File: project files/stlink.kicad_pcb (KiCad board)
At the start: 2 copper layers, 38.1 x 17.8 mm, 55 parts, among them J1 USB_C_Receptacle_USB2.0, J2 Sides, J3 SWD, Q1 MMBT9013, U1 STM32F103CBTx, U2 AMS1117-3.3, Y1 8MHz

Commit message: updates
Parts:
- removed C3: 20pF, Capacitor_SMD:C_0603_1608Metric
- removed R3: 100R, Resistor_SMD:R_0603_1608Metric_Pad1.05x0.95mm_HandSolder
- added C11: 22uF, Capacitor_Tantalum_SMD:CP_EIA-7343-30_AVX-N, B.Cu at (99.8, 166.4)
- added C7: 22uF, Capacitor_Tantalum_SMD:CP_EIA-7343-30_AVX-N, B.Cu at (99.8, 153.7)
- added F1: 1A, Fuse:Fuse_1210_3225Metric, B.Cu at (100.3, 118.0)
- added J4: TARGET, Connector_PinHeader_2.54mm:PinHeader_1x12_P2.54mm_Vertical, B.Cu at (105.4, 110.5)
- D1, D4, U2: moved to B.Cu
- J2: value Sides -> SELF; footprint Package_DIP:DIP-24_W15.24mm_Socket -> Connector_PinHeader_2.54mm:PinHeader_1x12_P2.54mm_Vertical; moved to B.Cu
- moved D1 60.6 mm to (101.6, 125.7), turned to 180 degrees
- moved U2 19.4 mm to (99.7, 160.0), turned to 180 degrees
- turned J2 to 270 degrees
- turned U1 to 180 degrees
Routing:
- net /D-: track 0.00 -> 2.72 mm
- net /D+: track 0.00 -> 2.71 mm

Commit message: ajfdlsa;jd;sakd
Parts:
- F1: footprint Fuse:Fuse_1210_3225Metric -> Fuse:Fuse_1206_3216Metric
- moved D3 56.5 mm to (100.3, 124.5)
- moved R12 56.3 mm to (100.3, 125.7)
- moved C13 28.1 mm to (121.0, 142.2)
- moved R6 23.2 mm to (133.7, 144.8)
- moved R5 13.7 mm to (133.7, 149.9)
- moved D1 5.02 mm to (100.3, 120.9), turned to 90 degrees
- moved F1 1.14 mm to (100.3, 116.8)
- turned R8 to 180 degrees
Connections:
- J2 pad 3: Self_SWDIOh -> Self_SWDCLKh
- J2 pad 5: Self_SWDCLKh -> Self_SWDIOh
- J4 pad 10: T_SWDCLKh -> T_SWDIOh
- J4 pad 11: T_SWOh -> T_NRST_SWDh
- J4 pad 12: T_NRST_SWDh -> T_SWOh
- J4 pad 8: T_SWDIOh -> T_SWDCLKh

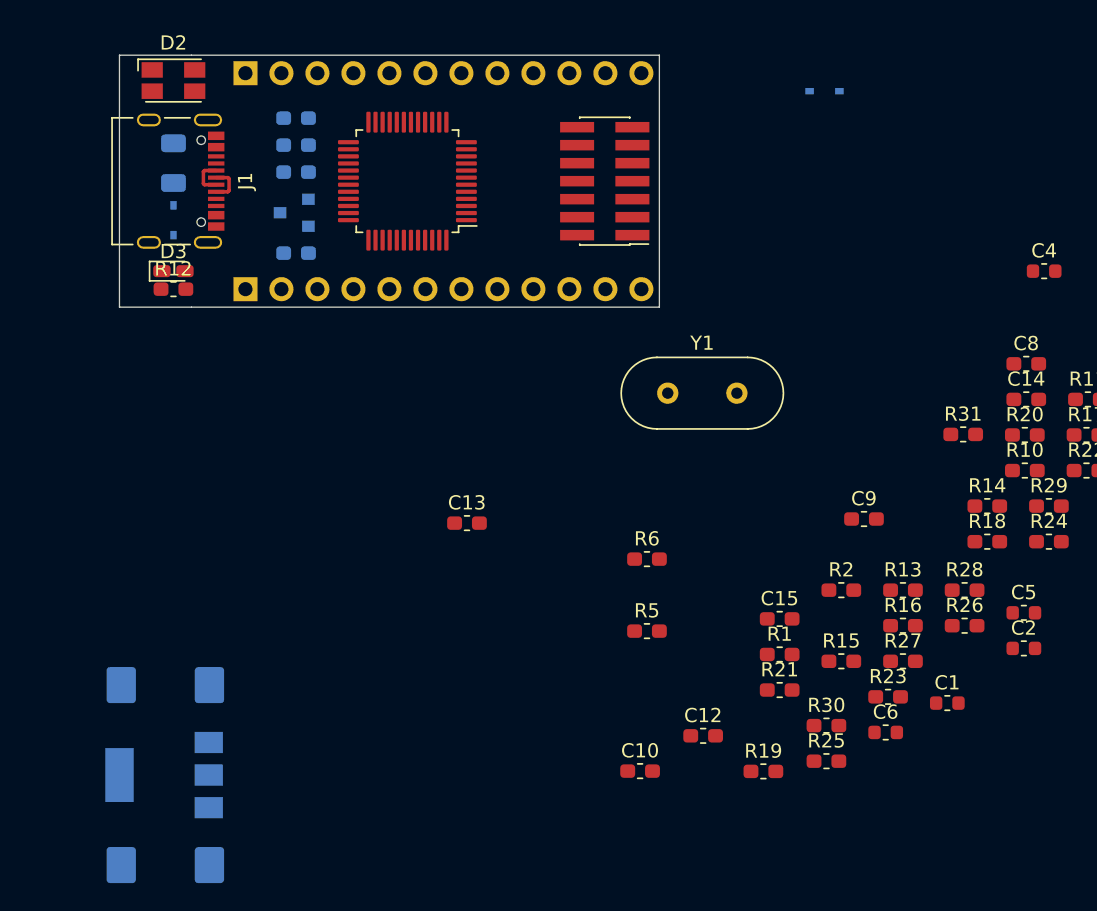
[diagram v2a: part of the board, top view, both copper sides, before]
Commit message: Added JTAG to STDC14
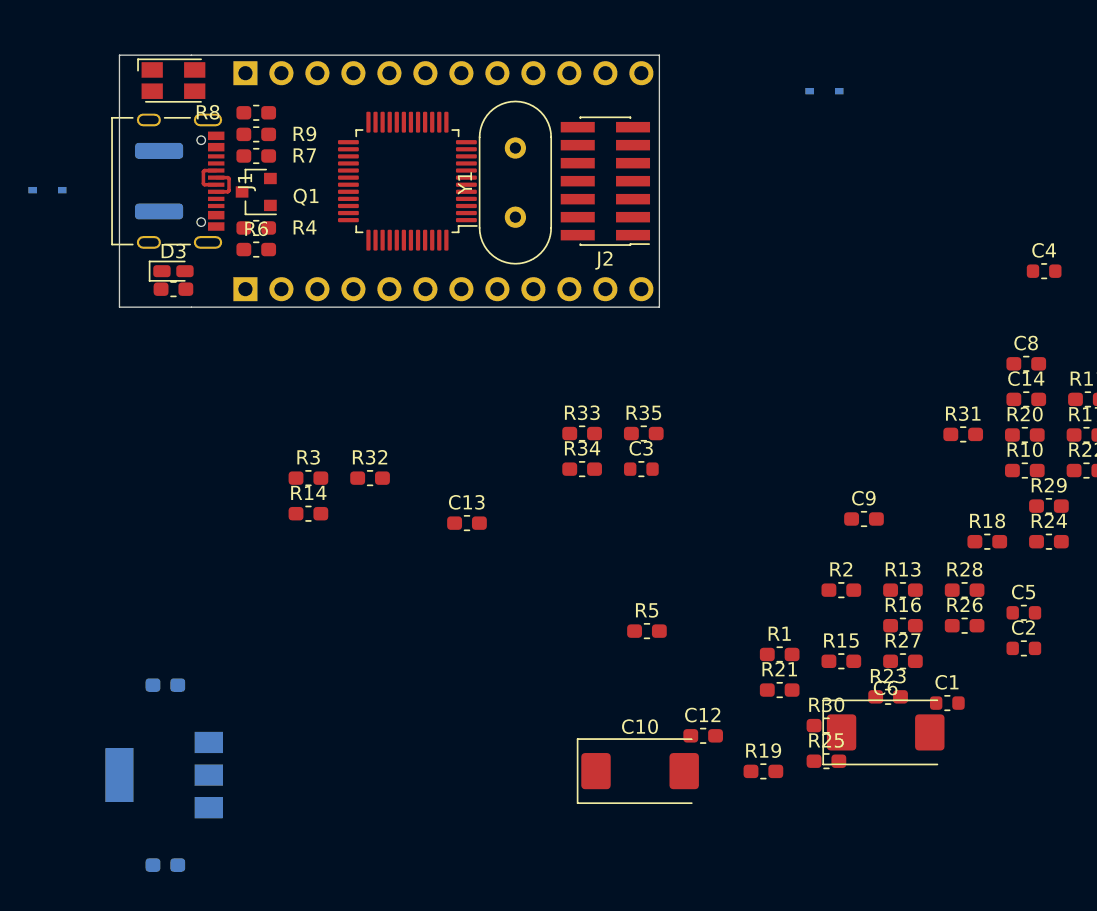
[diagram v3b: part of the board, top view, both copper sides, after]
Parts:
- removed C15: 100nF, Capacitor_SMD:C_0603_1608Metric_Pad1.05x0.95mm_HandSolder
- added C3: 100nF, Capacitor_SMD:C_0603_1608Metric, F.Cu at (133.3, 138.4)
- added R3: 10R, Resistor_SMD:R_0603_1608Metric_Pad1.05x0.95mm_HandSolder, F.Cu at (109.9, 139.1)
- added R32: 47R, Resistor_SMD:R_0603_1608Metric_Pad1.05x0.95mm_HandSolder, F.Cu at (114.2, 139.1)
- added R33: 47R, Resistor_SMD:R_0603_1608Metric_Pad1.05x0.95mm_HandSolder, F.Cu at (129.2, 135.9)
- added R34: 22R, Resistor_SMD:R_0603_1608Metric_Pad1.05x0.95mm_HandSolder, F.Cu at (129.2, 138.4)
- added R35: 22R, Resistor_SMD:R_0603_1608Metric_Pad1.05x0.95mm_HandSolder, F.Cu at (133.5, 135.9)
- C10: value 12pF -> 22uF; footprint Capacitor_SMD:C_0603_1608Metric_Pad1.05x0.95mm_HandSolder -> Capacitor_Tantalum_SMD:CP_EIA-7343-30_AVX-N
- C11: value 22uF -> 100nF; footprint Capacitor_Tantalum_SMD:CP_EIA-7343-30_AVX-N -> Capacitor_SMD:C_0603_1608Metric_Pad1.05x0.95mm_HandSolder
- C6: value 100nF -> 22uF; footprint Capacitor_SMD:C_0603_1608Metric -> Capacitor_Tantalum_SMD:CP_EIA-7343-30_AVX-N
- C7: value 22uF -> 12pF; footprint Capacitor_Tantalum_SMD:CP_EIA-7343-30_AVX-N -> Capacitor_SMD:C_0603_1608Metric_Pad1.05x0.95mm_HandSolder
- C8: value 12pF -> 100nF
- C9: value 100nF -> 12pF
- F1: footprint Fuse:Fuse_1206_3216Metric -> Fuse:Fuse_1812_4532Metric
- J2: value SELF -> SWD; footprint Connector_PinHeader_2.54mm:PinHeader_1x12_P2.54mm_Vertical -> Connector_PinHeader_1.27mm:PinHeader_2x07_P1.27mm_Vertical_SMD; moved to F.Cu
- J3: value SWD -> SELF; footprint Connector_PinHeader_1.27mm:PinHeader_2x07_P1.27mm_Vertical_SMD -> Connector_PinHeader_2.54mm:PinHeader_1x12_P2.54mm_Vertical; moved to B.Cu
- Q1, R4: moved to F.Cu
- R10: value 330R -> 36K
- R12: value 1K -> 330R
- R14: value 100K -> 1K
- R20, R21: value 220R -> 22R
- R22: value 100R -> 22R
- R23: value 10K -> 22R
- R24: value 10K -> 100R
- R25: value 680R -> 22R
- R26, R27: value 47R -> 220R
- R28: value 22R -> 680R
- R29, R30: value 22R -> 10K
- R7: value 10K -> 10R; moved to F.Cu
- R8: value 100R -> 10K; moved to F.Cu
- R9: value 36K -> 100R; moved to F.Cu
- moved R14 47.9 mm to (109.9, 141.6)
- moved R6 35.2 mm to (106.2, 122.9)
- moved J2 26.5 mm to (130.8, 118.1), turned to 180 degrees
- moved J3 26.5 mm to (105.4, 125.7), turned to 270 degrees
- moved Y1 16.4 mm to (124.5, 120.7), turned to 90 degrees
- moved D1 9.14 mm to (91.4, 118.7), turned to 180 degrees
- moved R4 3.32 mm to (106.2, 121.4)
- moved Q1 3.06 mm to (106.2, 118.9)
- moved R7 3.03 mm to (106.2, 116.3)
- moved R9 2.91 mm to (106.2, 114.8)
- moved R8 2.83 mm to (106.2, 113.3)
- moved F1 1.63 mm to (99.3, 118.1)
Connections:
- net Net-(U1-Pad19) renamed /T_JRST
- C10 pad 1: /STLINK_OST_OUT -> +3V3
- C12 pad 1: +3V3 -> BOOT_0h
- C13 pad 1: BOOT_0h -> Self_NRSTh
- C14 pad 1: Self_NRSTh -> /AIN
- C6 pad 1: +3V3 -> +5V
- C7 pad 1: +5V -> /STLINK_OSC_IN
- C8 pad 1: /STLINK_OSC_IN -> +5V
- C9 pad 1: +5V -> /STLINK_OST_OUT
- J2 pad 1: +5V -> Net-(J2-Pad1)
- J2 pad 10: Self_RXh -> T_JTDI(h)
- J2 pad 11: Self_TXh -> GND_detect(h)
- J2 pad 12: GNDREF -> T_NRST_SWDh
- J2 pad 2: +3V3 -> Net-(J2-Pad2)
- J2 pad 3: Self_SWDCLKh -> T_Vref
- J2 pad 4: GNDREF -> T_JTMS-T_SWDIO(h)
- J2 pad 5: Self_SWDIOh -> GNDREF
- J2 pad 6: Self_NRSTh -> T_JTLK(h)
- J2 pad 7: Self_SWOh -> GNDREF
- J2 pad 8: BOOT_0h -> T_JTDO-T_SWO(h)
- J2 pad 9: +3V3 -> T_JTLK(h)
- J3 pad 1: Net-(J3-Pad1) -> +5V
- J3 pad 10: Net-(J3-Pad10) -> Self_RXh
- J3 pad 11: GNDREF -> Self_TXh
- J3 pad 12: T_NRST_SWDh -> GNDREF
- J3 pad 2: Net-(J3-Pad2) -> +3V3
- J3 pad 3: T_Vref -> Self_SWDCLKh
- J3 pad 4: T_SWDIOh -> GNDREF
- J3 pad 5: GNDREF -> Self_SWDIOh
- J3 pad 6: T_SWDCLKh -> Self_NRSTh
- J3 pad 7: GNDREF -> Self_SWOh
- J3 pad 8: Net-(J3-Pad8) -> BOOT_0h
- J3 pad 9: Net-(J3-Pad9) -> +3V3
- R10 pad 1: Net-(D2-Pad3) -> GNDREF
- R10 pad 2: Self_TXh -> Net-(Q1-Pad1)
- R11 pad 1: Net-(D2-Pad1) -> Net-(D2-Pad3)
- R11 pad 2: Self_TXh -> /STLINK_LED
- R12 pad 1: Net-(D3-Pad2) -> Net-(D2-Pad1)
- R12 pad 2: +3V3 -> /STLINK_LED
- R13 pad 2: +3V3 -> GNDREF
- R14 pad 1: GNDREF -> Net-(D3-Pad2)
- R14 pad 2: /BOOT_1 -> +3V3
- R20 pad 1: /T_SWIM_IN -> T_NRST_SWDh
- R20 pad 2: /T_SWIM -> /T_NRST_SWD
- R21 pad 1: /T_NRST_SWIM_IN -> T_JTLK(h)
- R21 pad 2: /T_NRST_SWIM -> /T_JTCK
- R22 pad 1: /T_SWDIO_IN -> T_JTDO-T_SWO(h)
- R22 pad 2: /T_SWDIO -> /T_SWO
- R23 pad 1: /PC13 -> T_JTDO-T_SWO(h)
- R23 pad 2: GNDREF -> /T_JTDO
- R24 pad 1: /PC14 -> /T_SWDIO_IN
- R24 pad 2: GNDREF -> /T_JTMS
- R25 pad 1: /T_SWIM -> T_JTDI(h)
- R25 pad 2: +3V3 -> /T_JTDI
- R26 pad 1: /T_SWIM -> /T_SWIM_IN
- R26 pad 2: T_SWIMh -> /T_SWIM
- R27 pad 1: /T_NRST_SWIM -> /T_NRST_SWIM_IN
- R27 pad 2: T_NRST_SWIMh -> /T_NRST_SWIM
- R28 pad 1: T_NRST_SWDh -> /T_SWIM
- R28 pad 2: /T_NRST_SWD -> +3V3
- R29 pad 1: T_SWDCLKh -> /PC13
- R29 pad 2: /T_SWDCLK -> GNDREF
- R30 pad 1: T_SWDIOh -> /PC14
- R30 pad 2: /T_SWDIO -> GNDREF
- R31 pad 1: T_SWOh -> T_JTMS-T_SWDIO(h)
- R31 pad 2: Self_RXh -> /T_JTMS
- R7 pad 1: +5V -> /T_SWO
- R7 pad 2: Net-(Q1-Pad1) -> Self_RXh
- R8 pad 1: /USB_RENUMn -> +5V
- R9 pad 1: GNDREF -> /USB_RENUMn
- U1 pad 12: T_VCP_RXh -> /STLINK_TX
- U1 pad 13: T_VCP_TXh -> /STLINK_RX
- U1 pad 15: /T_SWDCLK -> /T_JTCK
- U1 pad 16: Net-(U1-Pad16) -> /T_JTDO
- U1 pad 17: Net-(U1-Pad17) -> /T_JTDI
- U1 pad 20: /BOOT_1 -> GNDREF
- U1 pad 26: /T_SWDCLK -> /T_JTCK
- U1 pad 27: /T_SWDIO -> /T_JTMS
- U1 pad 41: /T_SWIM_IN -> /T_NRST_SWIM_IN

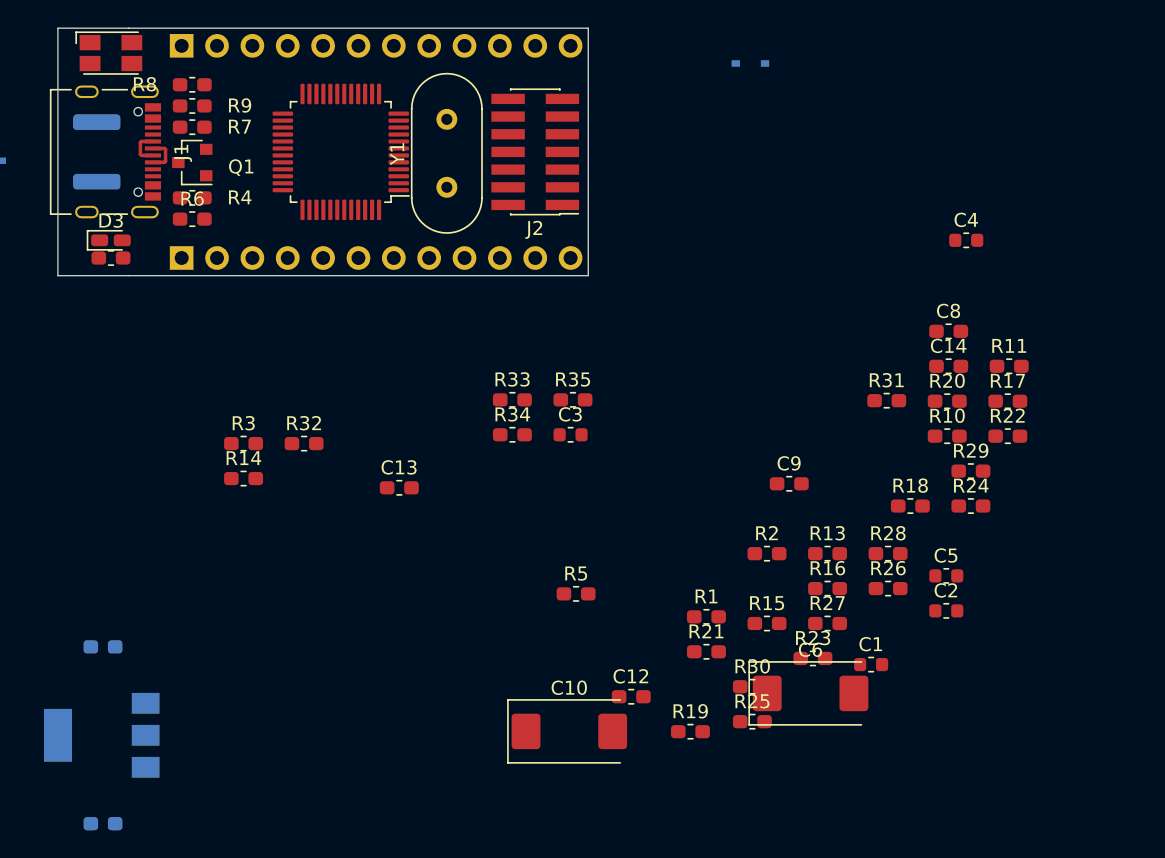
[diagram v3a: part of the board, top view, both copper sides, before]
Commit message: USB Type C shield fix
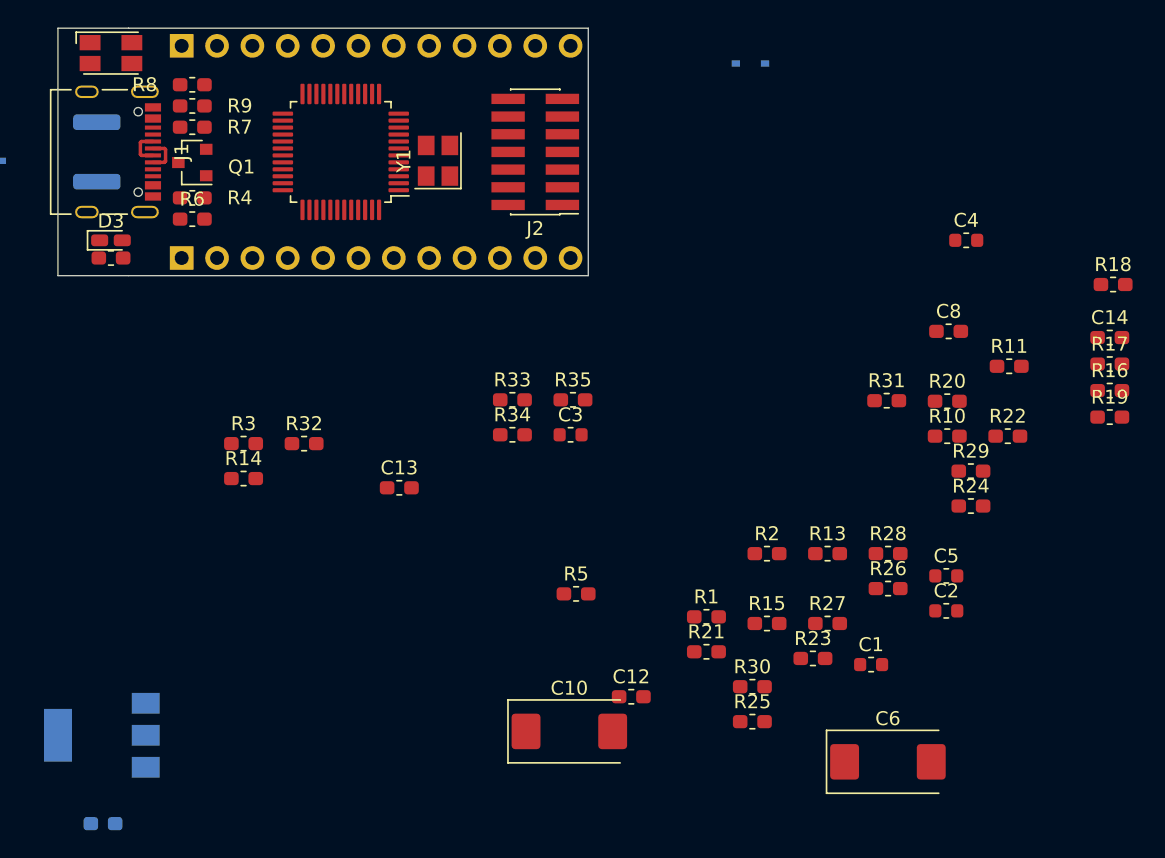
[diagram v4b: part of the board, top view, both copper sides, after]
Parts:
- C9: moved to B.Cu
- Y1: footprint Crystal:Crystal_HC49-4H_Vertical -> Crystal:Crystal_SMD_Abracon_ABM8G-4Pin_3.2x2.5mm
- moved C7 41.4 mm to (123.8, 120.0), turned to 180 degrees
- moved R19 37.7 mm to (172.1, 137.2)
- moved C9 35.2 mm to (123.8, 117.5)
- moved R16 24.8 mm to (172.1, 135.3)
- moved R18 21.6 mm to (172.3, 127.6)
- moved C14 11.8 mm to (172.1, 131.4)
- moved R17 7.80 mm to (172.1, 133.3)
- moved C6 7.42 mm to (156.1, 161.9)
- moved Y1 2.01 mm to (123.8, 118.7)
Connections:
- Y1 pad 2: /STLINK_OST_OUT -> Net-(Y1-Pad2)
